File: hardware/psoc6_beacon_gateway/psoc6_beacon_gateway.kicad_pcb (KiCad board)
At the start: 2 copper layers, 68.8 x 53.6 mm, 23 parts, among them J1 Conn_01x02_Female, J2 Conn_01x02_Female, J3 Conn_01x02_Female, Q1 BT136-800, Q2 BT136-800, U1 MOC3063M, U2 MOC3063M

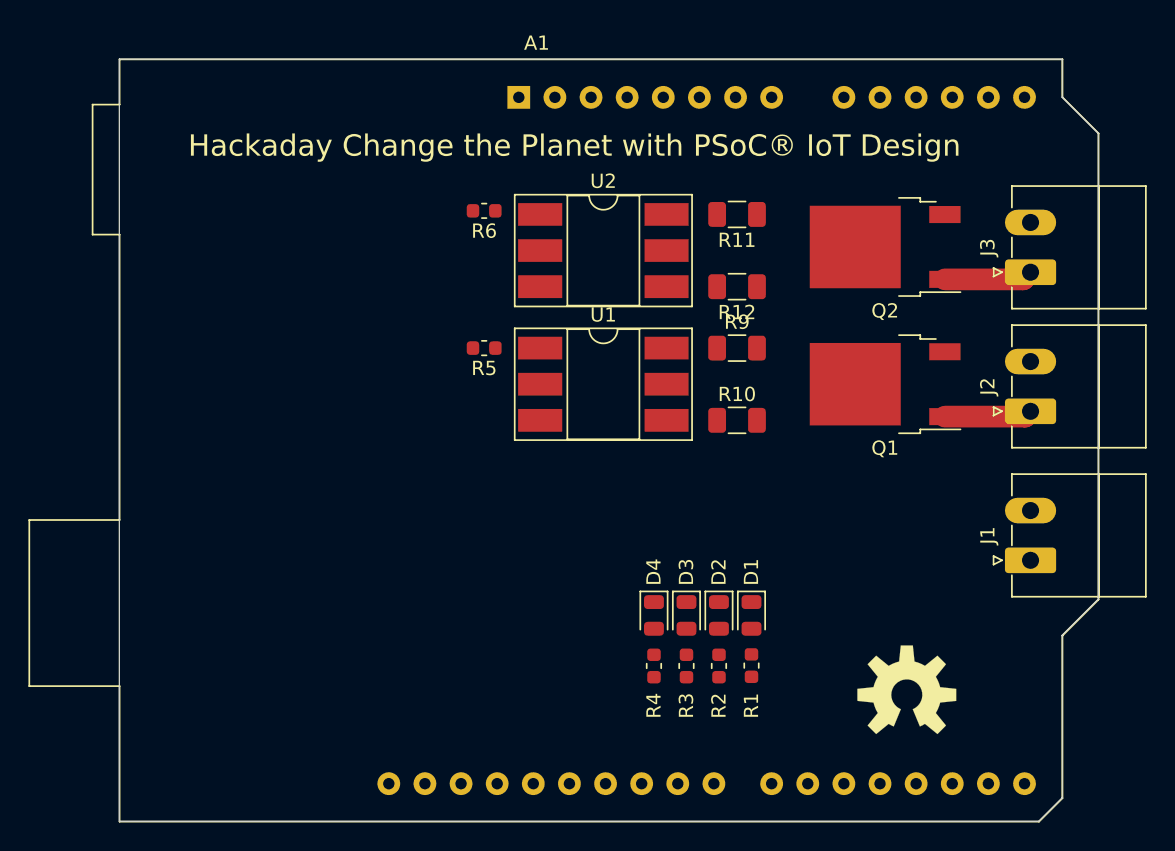
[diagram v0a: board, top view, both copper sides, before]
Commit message: FW with some issues on BLE and WiFi at same time
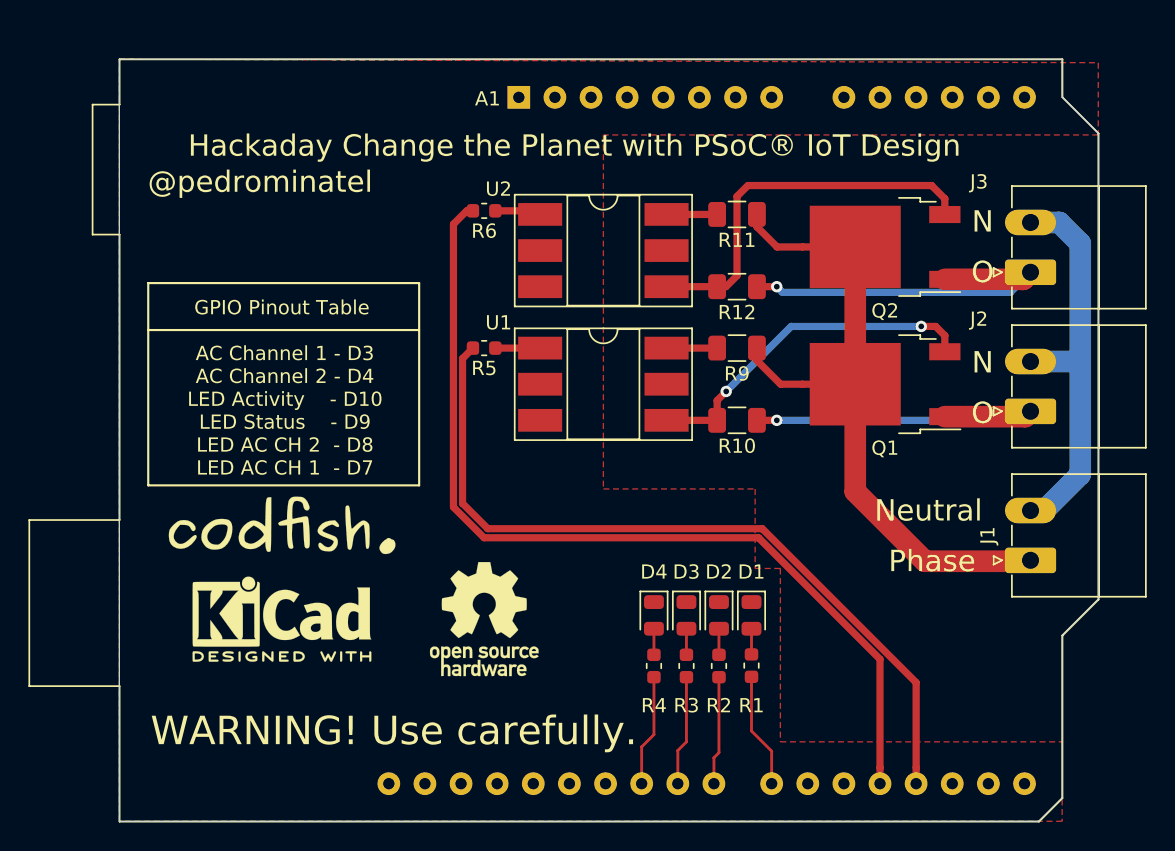
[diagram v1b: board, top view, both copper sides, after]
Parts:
- removed ?: , Aesthetics:OSHW-LOGO-L
- added G***: LOGO, logos:codfish_03, F.Cu at (-81.0, 23.4)
- added REF**: KiCad-Logo2_5mm_SilkScreen, Symbol:KiCad-Logo2_5mm_SilkScreen, F.Cu at (-81.0, 30.0)
- added REF**: OSHW-Logo_7.5x8mm_SilkScreen, Symbol:OSHW-Logo_7.5x8mm_SilkScreen, F.Cu at (-66.8, 30.0)
- turned R10 to 180 degrees
- turned R9 to 180 degrees
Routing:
- net CH2_CONTROL: track 0.00 -> 64.8 mm
- net CH1_CONTROL: track 0.00 -> 55.5 mm
- net AC_PHA_IN: track 0.00 -> 48.4 mm
- net NEUTRAL: track 0.00 -> 28.5 mm
- net Net-(Q2-Pad3): track 0.00 -> 27.3 mm
- net Net-(Q1-Pad3): track 0.00 -> 24.5 mm, vias 0 -> 2
- net CH2_AC_OUT: track 6.23 -> 26.2 mm, vias 0 -> 1
- net CH1_AC_OUT: track 6.18 -> 25.7 mm, vias 0 -> 1
- net LED_CH1: track 0.00 -> 8.10 mm
- net LED_ACTIVITY: track 0.00 -> 7.85 mm
- net LED_STATUS: track 0.00 -> 7.74 mm
- net LED_CH2: track 0.00 -> 7.64 mm
- net Net-(R9-Pad2): track 0.00 -> 3.55 mm
- net Net-(R11-Pad2): track 0.00 -> 3.55 mm
- net Net-(R6-Pad1): track 0.00 -> 3.25 mm
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- added copper zone on F.Cu, net GND
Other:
- board text added: "@pedrominatel"
- board text added: "GPIO Pinout Table AC Channel 1 - D3 AC Channel 2 - D4 LED Activity - D10 LED Status - D9 LED AC CH 2 - D8 LED AC CH 1 - D7"
- board text added: "N"
- board text added: "Neutral"
- board text added: "O"
- board text added: "Phase"
- board text added: "WARNING! Use carefully."
